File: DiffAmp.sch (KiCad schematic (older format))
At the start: 39 parts, among them J1 IN+, J10 Screw_Terminal_01x01, J2 IN-, J3 GND, J4 BARREL_JACK, J5 Screw_Terminal_01x01, J6 Screw_Terminal_01x01, J7 Screw_Terminal_01x01, J8 Screw_Terminal_01x01, J9 Screw_Terminal_01x01, U1 SF_IHXXXXS, U2 TPS7A49, U3 TPS7A30, U4 OPA189

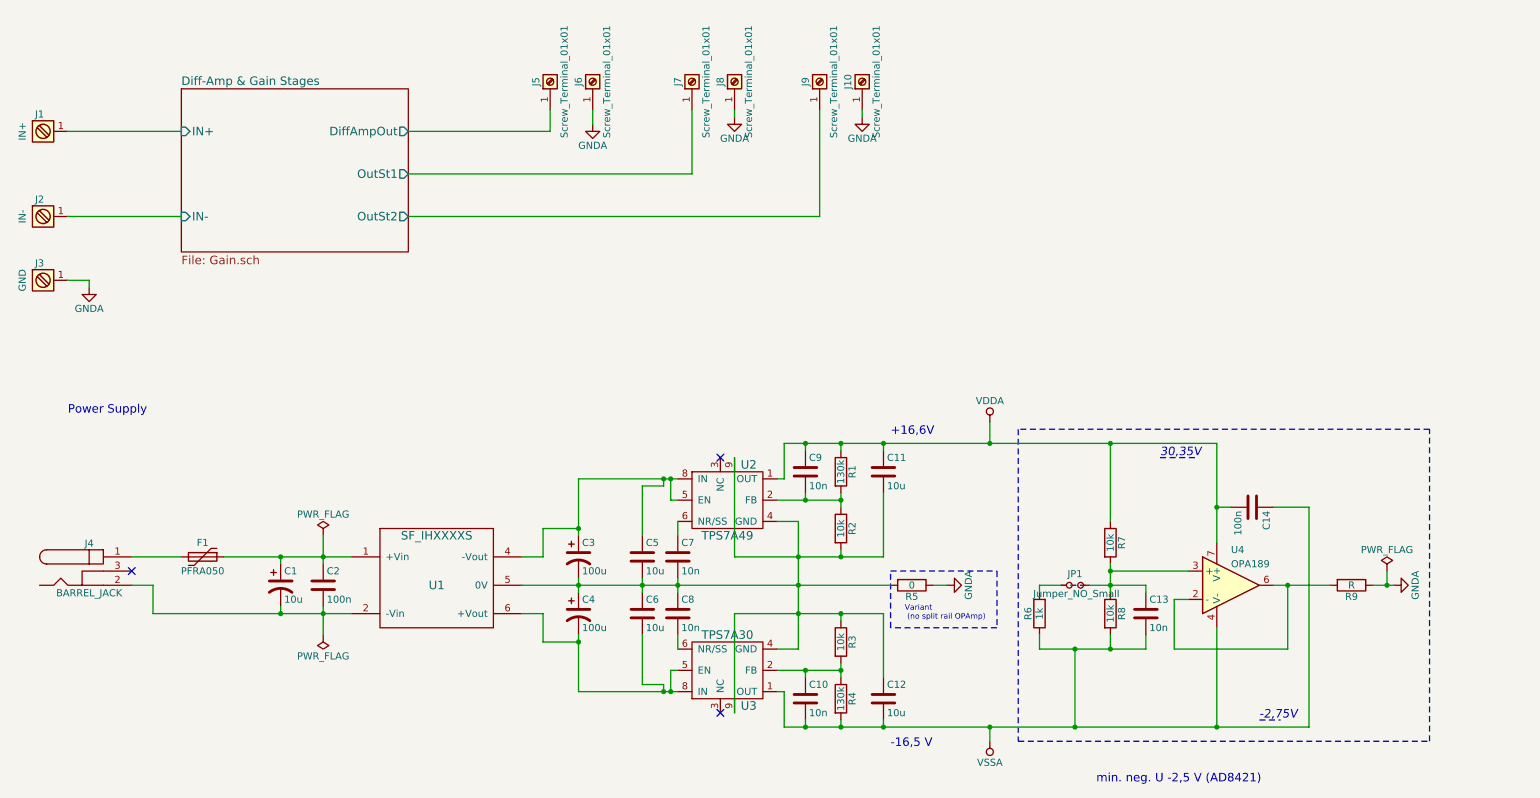
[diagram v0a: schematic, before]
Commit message: Schematic rearranged Added Netlist
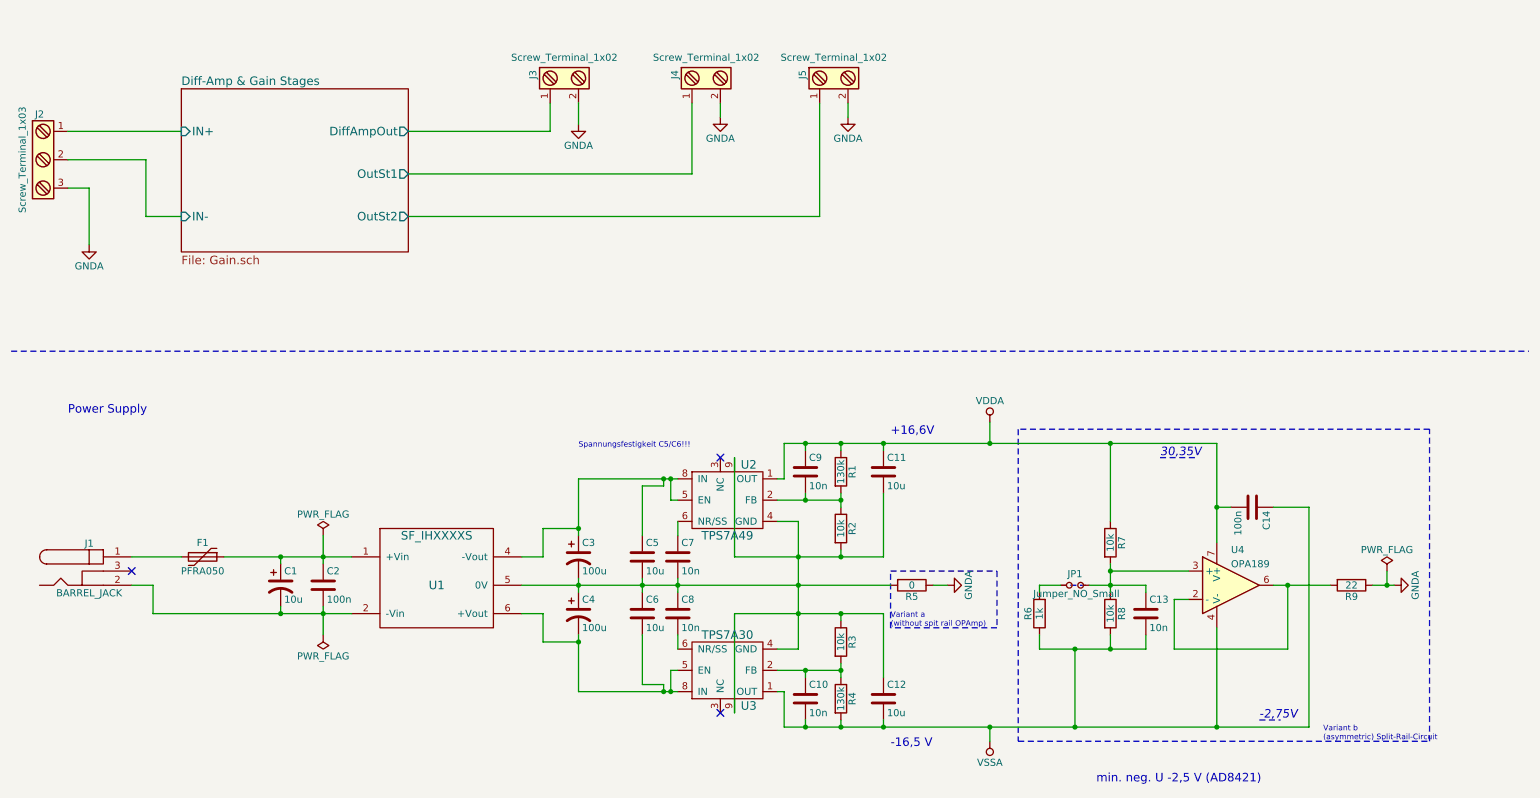
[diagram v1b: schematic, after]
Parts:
- removed J1: IN+, symbol Screw_Terminal_1x01
- removed J10, J5, J6, J7, J8, J9: Screw_Terminal_01x01, symbol Screw_Terminal_01x01
- removed J2: IN-, symbol Screw_Terminal_1x01
- removed J3: GND, symbol Screw_Terminal_1x01
- added J2: Screw_Terminal_1x03, Connectors_Terminal_Blocks:TerminalBlock_bornier-3_P5.08mm, symbol Screw_Terminal_1x03
- added J3, J4, J5: Screw_Terminal_1x02, Connectors_Terminal_Blocks:TerminalBlock_bornier-2_P5.08mm, symbol Screw_Terminal_1x02
- C1: footprint (none) -> Capacitors_THT:CP_Radial_D5.0mm_P2.00mm
- C10, C13, C14, C2, C7, C8, C9: footprint (none) -> Capacitors_SMD:C_0805
- C11, C12, C5, C6: footprint (none) -> Capacitors_SMD:C_1210
- C3, C4: footprint (none) -> Capacitors_THT:CP_Radial_D8.0mm_P3.50mm
- F1: footprint (none) -> Resistors_THT:R_Axial_DIN0204_L3.6mm_D1.6mm_P5.08mm_Horizontal
- J1: renamed from J4; footprint (none) -> Connectors:BARREL_JACK
- JP1: footprint (none) -> Pin_Headers:Pin_Header_Straight_1x02_Pitch2.54mm
- R1, R2, R3, R4, R5, R6, R7, R8: footprint (none) -> Resistors_SMD:R_0805
- R9: value R -> 22; footprint (none) -> Resistors_SMD:R_0805
- U1: footprint (none) -> Converters_DCDC_ACDC:DCDC-Conv_TRACO_TMR_1-xxxx_Dual
- U2, U3: footprint (none) -> Housings_SSOP:MSOP-8-1EP_3x3mm_Pitch0.65mm
- U4: footprint (none) -> Housings_SOIC:SOIC-8_3.9x4.9mm_Pitch1.27mm
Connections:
- net Diff-Amp & Gain Stages/DiffAmpOut: now also J3.1
- net Diff-Amp & Gain Stages/IN+: now also J2.1
- net Diff-Amp & Gain Stages/IN-: now also J2.2
- net Diff-Amp & Gain Stages/OutSt1: now also J4.1
- net Diff-Amp & Gain Stages/OutSt2: now also J5.1
- net GNDA: now also J2.3, J3.2, J4.2, J5.2
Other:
- note added: "Spannungsfestigkeit C5/C6!!!\n\n"
- note added: "Variant a\n(without spit rail OPAmp)"
- note added: "Variant b\n(asymmetric) Split-Rail-Circuit"
- note removed: "Variant\n (no split rail OPAmp)"

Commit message: Parts placed on PCB
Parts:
- removed J1: BARREL_JACK, Connectors:BARREL_JACK, symbol BARREL_JACK
- removed J3, J4, J5: Screw_Terminal_1x02, Connectors_Terminal_Blocks:TerminalBlock_bornier-2_P5.08mm, symbol Screw_Terminal_1x02
- added J1: USB_OTG, DiffAmp:MIC_USB_BBU, symbol USB_OTG
- added J3, J4, J5: Conn_01x02, Pin_Headers:Pin_Header_Straight_1x02_Pitch2.54mm, symbol Conn_01x02
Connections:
- net Diff-Amp & Gain Stages/DiffAmpOut: now also J3.1 (Pin_1)
- net Diff-Amp & Gain Stages/OutSt1: now also J4.1 (Pin_1)
- net Diff-Amp & Gain Stages/OutSt2: now also J5.1 (Pin_1)
- net GNDA: now also J3.2 (Pin_2), J4.2 (Pin_2)
- net at C1.2, C2.2, U1.2 (-Vin): now also J1.5 (GND)
- net at C3.1, C5.1, U2.5 (EN)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: now also U1.6 (+Vout); no longer U1.4 (-Vout)
- net at C4.2, C6.2, U3.5 (EN)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: now also U1.4 (-Vout); no longer U1.6 (+Vout)
- net at F1.2: now also J1.1 (VBUS)
- no-connect marks 3 -> 6
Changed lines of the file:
@@
-$EndComp
-$Comp
-L BARREL_JACK J1
-U 1 1 5A9DB8C2
-P 1050 4600
-F 0 "J1" H 1050 4795 50  0000 C CNN
-F 1 "BARREL_JACK" H 1050 4445 50  0000 C CNN
-F 2 "Connectors:BARREL_JACK" H 1050 4600 50  0001 C CNN
-F 3 "" H 1050 4600 50  0001 C CNN
-	1    1050 4600
-	1    0    0    -1
 $EndComp
 $Comp
@@
 L GNDA #PWR06
 U 1 1 5AA10804
-P 4500 1450
-F 0 "#PWR06" H 4500 1200 50  0001 C CNN
-F 1 "GNDA" H 4500 1300 50  0000 C CNN
-F 2 "" H 4500 1450 50  0001 C CNN
-F 3 "" H 4500 1450 50  0001 C CNN
-	1    4500 1450
+P 4400 1450
+F 0 "#PWR06" H 4400 1200 50  0001 C CNN
+F 1 "GNDA" H 4400 1300 50  0000 C CNN
+F 2 "" H 4400 1450 50  0001 C CNN
+F 3 "" H 4400 1450 50  0001 C CNN
+	1    4400 1450
 	1    0    0    -1
 $EndComp
@@
 L GNDA #PWR07
 U 1 1 5AA10C9C
-P 5500 1400
-F 0 "#PWR07" H 5500 1150 50  0001 C CNN
-F 1 "GNDA" H 5500 1250 50  0000 C CNN
-F 2 "" H 5500 1400 50  0001 C CNN
-F 3 "" H 5500 1400 50  0001 C CNN
-	1    5500 1400
+P 5400 1400
+F 0 "#PWR07" H 5400 1150 50  0001 C CNN
+F 1 "GNDA" H 5400 1250 50  0000 C CNN
+F 2 "" H 5400 1400 50  0001 C CNN
+F 3 "" H 5400 1400 50  0001 C CNN
+	1    5400 1400
 	1    0    0    -1
 $EndComp
@@
 L GNDA #PWR08
 U 1 1 5AA11818
-P 6400 1400
-F 0 "#PWR08" H 6400 1150 50  0001 C CNN
-F 1 "GNDA" H 6400 1250 50  0000 C CNN
-F 2 "" H 6400 1400 50  0001 C CNN
-F 3 "" H 6400 1400 50  0001 C CNN
-	1    6400 1400
-	1    0    0    -1
-$EndComp
-NoConn ~ 1350 4600
+P 6300 1350
+F 0 "#PWR08" H 6300 1100 50  0001 C CNN
+F 1 "GNDA" H 6300 1200 50  0000 C CNN
+F 2 "" H 6300 1350 50  0001 C CNN
+F 3 "" H 6300 1350 50  0001 C CNN
+	1    6300 1350
+	1    0    0    -1
+$EndComp
 $Comp
 L PWR_FLAG #FLG09
@@
 	2000 4500 2900 4500
 Wire Wire Line
-	1350 4700 1500 4700
-Wire Wire Line
-	1500 4700 1500 4900
-Wire Wire Line
 	1500 4900 2900 4900
 Wire Wire Line
@@
 Connection ~ 2700 4900
 Wire Wire Line
-	4100 4500 4250 4500
-Wire Wire Line
-	4250 4300 4500 4300
-Wire Wire Line
 	4500 3950 4500 4350
-Wire Wire Line
-	4250 4500 4250 4300
 Wire Wire Line
 	4100 4700 6700 4700
@@
 Connection ~ 4500 4700
 Wire Wire Line
-	4100 4900 4250 4900
-Wire Wire Line
-	4250 4900 4250 5100
-Wire Wire Line
-	4250 5100 4500 5100
+	4200 5100 4500 5100
 Wire Wire Line
 	4500 5050 4500 5450
@@
 	9300 5650 9450 5650
 Wire Wire Line
-	1700 4500 1350 4500
+	1250 4500 1700 4500
 Wire Wire Line
 	1050 1900 1050 2300
@@
 	5300 1300 5300 1800
 Wire Wire Line
-	4500 1300 4500 1450
-Wire Wire Line
-	5500 1300 5500 1400
+	4400 1300 4400 1450
+Wire Wire Line
+	5400 1300 5400 1400
 Wire Wire Line
 	6200 1300 6200 2100
@@
 Wire Wire Line
 	1700 1500 900  1500
-$Comp
-L Screw_Terminal_1x02 J3
-U 1 1 5AABACF6
-P 4400 1100
-F 0 "J3" H 4400 1350 50  0000 C TNN
-F 1 "Screw_Terminal_1x02" V 4250 1100 50  0000 C TNN
-F 2 "Connectors_Terminal_Blocks:TerminalBlock_bornier-2_P5.08mm" H 4400 875 50  0001 C CNN
-F 3 "" H 4375 1100 50  0001 C CNN
-	1    4400 1100
-	0    -1   1    0
-$EndComp
 $Comp
 L Screw_Terminal_1x03 J2
@@
 Wire Wire Line
 	900  1900 1050 1900
-$Comp
-L Screw_Terminal_1x02 J4
-U 1 1 5AABBFAC
-P 5400 1100
-F 0 "J4" H 5400 1350 50  0000 C TNN
-F 1 "Screw_Terminal_1x02" V 5250 1100 50  0000 C TNN
-F 2 "Connectors_Terminal_Blocks:TerminalBlock_bornier-2_P5.08mm" H 5400 875 50  0001 C CNN
-F 3 "" H 5375 1100 50  0001 C CNN
-	1    5400 1100
-	0    -1   1    0
-$EndComp
-$Comp
-L Screw_Terminal_1x02 J5
-U 1 1 5AABC3D9
-P 6300 1100
-F 0 "J5" H 6300 1350 50  0000 C TNN
-F 1 "Screw_Terminal_1x02" V 6150 1100 50  0000 C TNN
-F 2 "Connectors_Terminal_Blocks:TerminalBlock_bornier-2_P5.08mm" H 6300 875 50  0001 C CNN
-F 3 "" H 6275 1100 50  0001 C CNN
-	1    6300 1100
-	0    -1   1    0
-$EndComp
-Wire Wire Line
-	6400 1300 6400 1400
+Wire Wire Line
+	6300 1250 6300 1350
+$Comp
+L USB_OTG J1
+U 1 1 5AAC0628
+P 950 4700
+F 0 "J1" H 750 5150 50  0000 L CNN
+F 1 "USB_OTG" H 750 5050 50  0000 L CNN
+F 2 "DiffAmp:MIC_USB_BBU" H 1100 4650 50  0001 C CNN
+F 3 "" H 1100 4650 50  0001 C CNN
+	1    950  4700
+	1    0    0    -1
+$EndComp
+Wire Wire Line
+	950  5100 950  5150
+Wire Wire Line
+	950  5150 1500 5150
+Wire Wire Line
+	1500 5150 1500 4900
+NoConn ~ 1250 4700
+NoConn ~ 1250 4800
+NoConn ~ 1250 4900
+NoConn ~ 850  5100
+Wire Wire Line
+	4200 4500 4200 5100
+Wire Wire Line
+	4200 4500 4100 4500
+Wire Wire Line
+	4300 4900 4100 4900
+Wire Wire Line
+	4300 4300 4300 4900
+Wire Wire Line
+	4300 4300 4500 4300
+$Comp
+L Conn_01x02 J3
+U 1 1 5AAC1A50
+P 4300 1100
+F 0 "J3" H 4300 1200 50  0000 C CNN
+F 1 "Conn_01x02" H 4300 900 50  0000 C CNN
+F 2 "Pin_Headers:Pin_Header_Straight_1x02_Pitch2.54mm" H 4300 1100 50  0001 C CNN
+F 3 "" H 4300 1100 50  0001 C CNN
+	1    4300 1100
+	0    -1   -1   0
+$EndComp
+$Comp
+L Conn_01x02 J4
+U 1 1 5AAC1D4B
+P 5300 1100
+F 0 "J4" H 5300 1200 50  0000 C CNN
+F 1 "Conn_01x02" H 5300 900 50  0000 C CNN
+F 2 "Pin_Headers:Pin_Header_Straight_1x02_Pitch2.54mm" H 5300 1100 50  0001 C CNN
+F 3 "" H 5300 1100 50  0001 C CNN
+	1    5300 1100
+	0    -1   -1   0
+$EndComp
+$Comp
+L Conn_01x02 J5
+U 1 1 5AAC1DFE
+P 6200 1100
+F 0 "J5" H 6200 1200 50  0000 C CNN
+F 1 "Conn_01x02" H 6200 900 50  0000 C CNN
+F 2 "Pin_Headers:Pin_Header_Straight_1x02_Pitch2.54mm" H 6200 1100 50  0001 C CNN
+F 3 "" H 6200 1100 50  0001 C CNN
+	1    6200 1100
+	0    -1   -1   0
+$EndComp
 $EndSCHEMATC

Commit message: Begin Layouting
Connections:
- net GNDA: now also J5.2 (Pin_2)
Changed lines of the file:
@@
 L GNDA #PWR08
 U 1 1 5AA11818
-P 6300 1350
-F 0 "#PWR08" H 6300 1100 50  0001 C CNN
-F 1 "GNDA" H 6300 1200 50  0000 C CNN
-F 2 "" H 6300 1350 50  0001 C CNN
-F 3 "" H 6300 1350 50  0001 C CNN
-	1    6300 1350
+P 6300 1400
+F 0 "#PWR08" H 6300 1150 50  0001 C CNN
+F 1 "GNDA" H 6300 1250 50  0000 C CNN
+F 2 "" H 6300 1400 50  0001 C CNN
+F 3 "" H 6300 1400 50  0001 C CNN
+	1    6300 1400
 	1    0    0    -1
 $EndComp
@@
 	900  1900 1050 1900
 Wire Wire Line
-	6300 1250 6300 1350
+	6300 1300 6300 1400
 $Comp
 L USB_OTG J1

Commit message: Schematic pdf, Layout pdf + Gerber added
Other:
- note removed: "Spannungsfestigkeit C5/C6!!!\n\n"
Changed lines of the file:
@@
 Text Notes 9750 5800 0    39   ~ 0
 Variant b\n(asymmetric) Split-Rail-Circuit
-Text Notes 4500 3800 0    39   ~ 0
-Spannungsfestigkeit C5/C6!!!\n\n
 Wire Wire Line
 	2000 4500 2900 4500

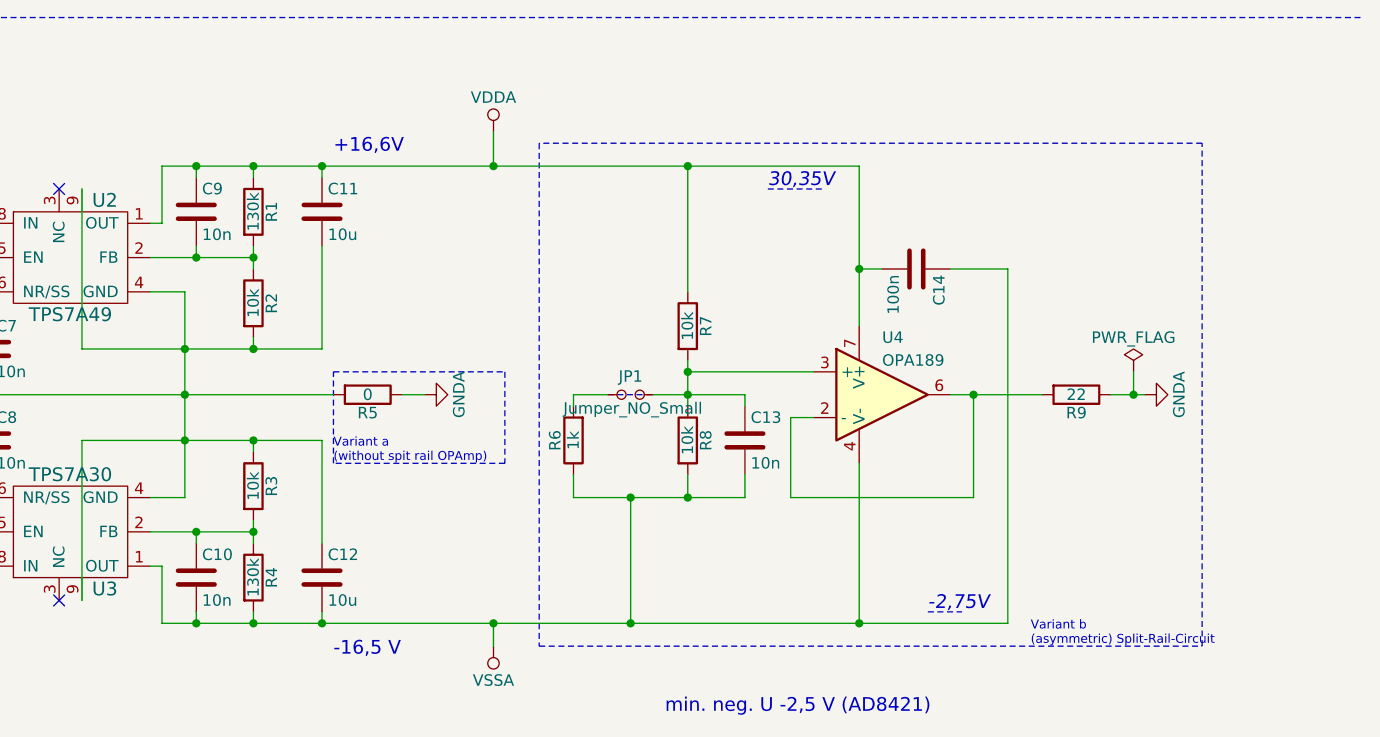
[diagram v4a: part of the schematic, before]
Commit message: Changed GNDA-"Generation" on Schematic and Board
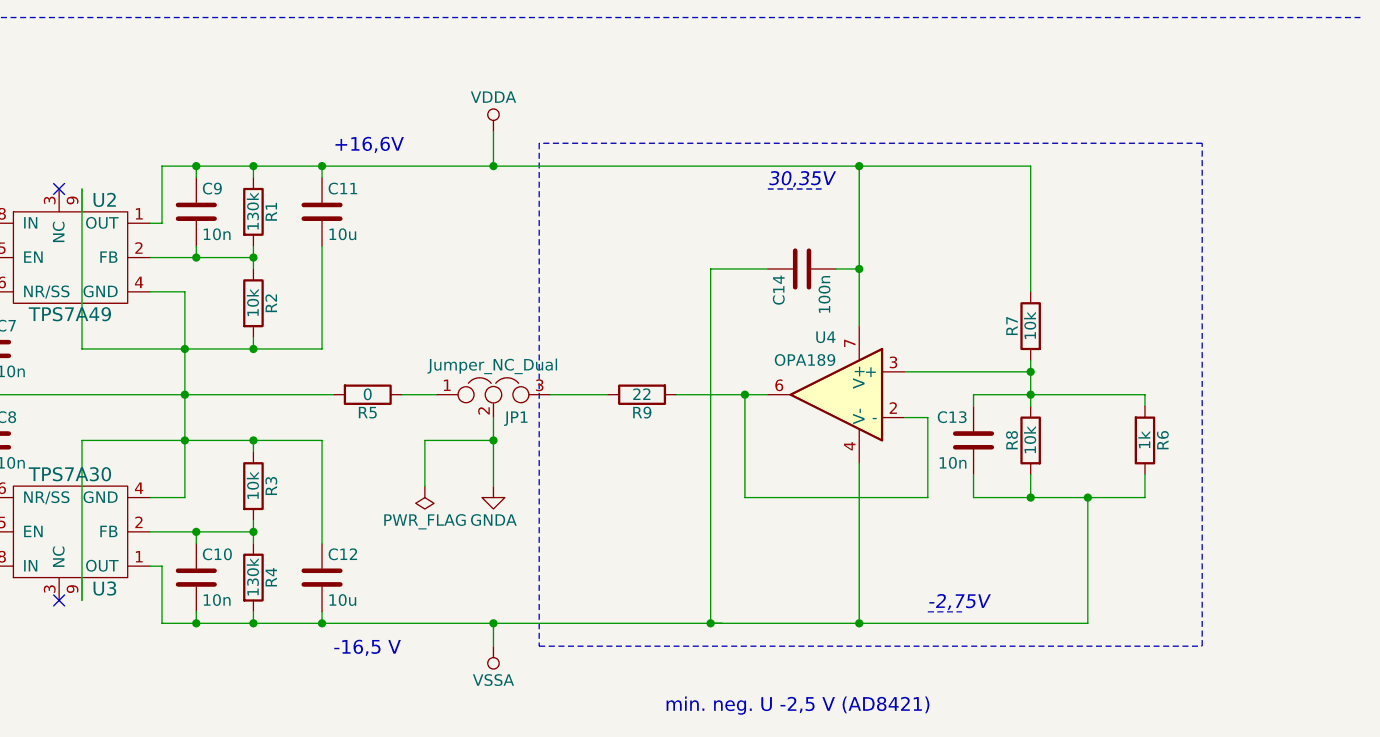
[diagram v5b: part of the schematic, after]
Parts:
- removed JP1: Jumper_NO_Small, Pin_Headers:Pin_Header_Straight_1x02_Pitch2.54mm, symbol Jumper_NO_Small
- added JP1: Jumper_NC_Dual, Pin_Headers:Pin_Header_Straight_1x03_Pitch2.54mm, symbol Jumper_NC_Dual
- F1: footprint Resistors_THT:R_Axial_DIN0204_L3.6mm_D1.6mm_P5.08mm_Horizontal -> Resistors_ThroughHole:R_Axial_DIN0204_L3.6mm_D1.6mm_P5.08mm_Horizontal
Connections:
- net GNDA: now also JP1.2; no longer R5.1, R9.1
- net at C13.1, R7.2, R8.1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: now also R6.2
- new net: JP1.1, R5.1
- new net: JP1.3, R9.1
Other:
- note removed: "Variant a\n(without spit rail OPAmp)"
- note removed: "Variant b\n(asymmetric) Split-Rail-Circuit"
- moved on the sheet: C13, C14, R6, R7, R8, R9, U4
